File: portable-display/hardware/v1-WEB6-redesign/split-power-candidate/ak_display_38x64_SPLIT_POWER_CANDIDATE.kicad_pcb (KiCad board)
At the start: 4 copper layers, 38 x 64 mm, 125 parts, among them J1 USB4105-GF-A-060, J2 1S LiPo + NTC, J3 DEBUG POGO, J4 KD024EGOIN152-01, J5 MicroSD, Q1 2N7002, Q2 2N7002, Q3 AO3401A, SW1 UP, SW2 DOWN, SW3 OK, SW4 BACK, SW5 POWER, SW6 FEL, U1 AXP2101, U10 TPS65631DPDR, U11 SN74LVC2G17DBVR, U2 V851s, U4 LIS2DW12TR, U5 RV-3028-C7, U6 SN74LVC1G123DCTR, U8 TPS22918DBVR, U9 USBLC6-2SC6, Y1 24MHz 10ppm

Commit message: fix(pcb): add C53 1uF (C52923) + C54 100nF (C1525) at U8 TPS22918 VIN
Both JLC basic 0402, F.Cu, GND via outside pad (>=0.15 mm pad-to-hole).
Schematic regenerated; DRC/parity/ERC 0.
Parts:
- added C53: 1u, Sameat:0402, F.Cu at (5.47, 35.1)
- added C54: 100n, Sameat:0402, F.Cu at (2.75, 36.4)
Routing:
- net GND: track 14.4 -> 16.3 mm, vias 60 -> 62
- net 3V3: track 161.2 -> 161.9 mm

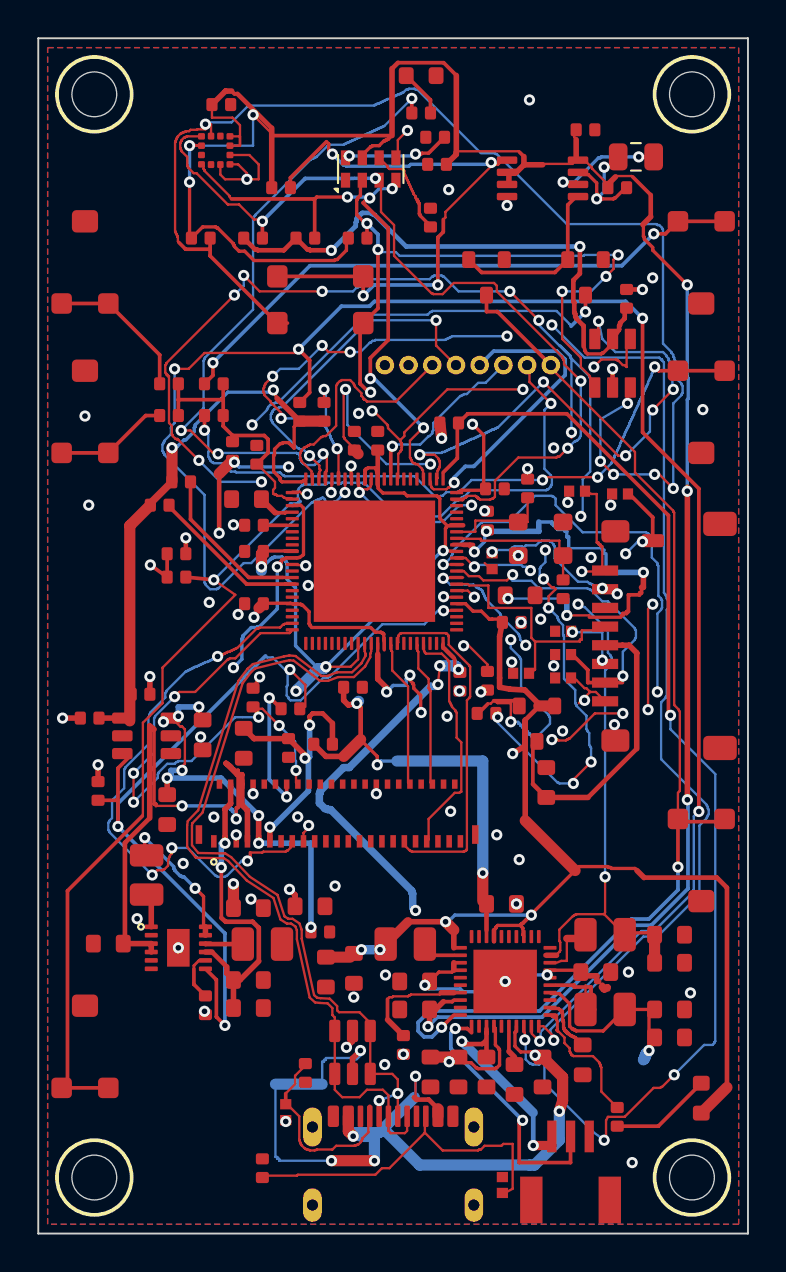
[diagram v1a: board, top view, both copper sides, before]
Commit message: feat(j5): swap microSD to in-stock XKTF-0803-0, TPD4E05U06 flow-through ESD, reroute SD bus off Y1
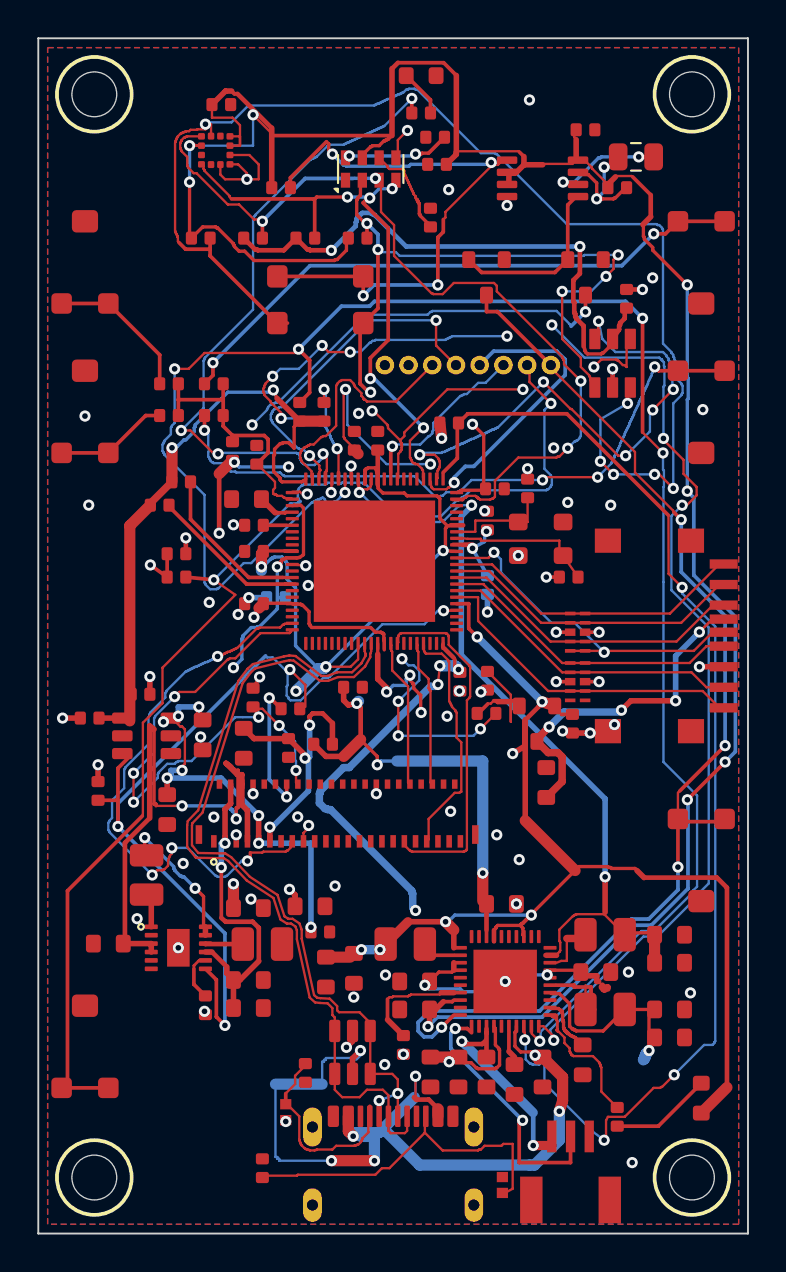
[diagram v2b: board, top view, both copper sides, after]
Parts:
- removed D10, D11, D12, D6, D7, D8, D9: ESDLC5V0LB, Sameat:DFN1006-2
- added C57: 100n, Sameat:0402, B.Cu at (12.7, 29.9)
- added U12: TPD4E05U06DQAR, Sameat:TPD4E05U06_DQA, F.Cu at (28.9, 31.8)
- added U13: TPD4E05U06DQAR, Sameat:TPD4E05U06_DQA, F.Cu at (28.9, 34.5)
- C34: footprint Sameat:0603 -> Sameat:0402; moved to B.Cu
- J5: footprint Sameat:MICROSD -> Sameat:XKTF-0803-0
- moved C14 6.32 mm to (28.6, 36.7), turned to 90 degrees
- moved C34 1.83 mm to (24.1, 29.3), turned to -90 degrees
- moved J5 1.10 mm to (33.6, 32.0)
- moved C13 0.72 mm to (28.4, 28.9), turned to 180 degrees
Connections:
- C14 pad 1: 3V3 -> GND
- C14 pad 2: GND -> 3V3
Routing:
- net SD_PWR_EN: track 79.2 -> 22.1 mm, vias 16 -> 5
- net SOC_LDO_1V8: track 26.7 -> 5.31 mm, vias 5 -> 2
- net SD_D0: track 34.3 -> 16.5 mm, vias 8 -> 0
- net SD_D2: track 31.5 -> 16.5 mm, vias 3 -> 0
- net SD_PWR_GATE: track 18.3 -> 7.96 mm, vias 3 -> 0
- net GND: track 16.3 -> 23.6 mm, vias 62 -> 67
- net DRAM_1V5: track 54.1 -> 58.7 mm, vias 7 -> 5
- net SD_DET: track 15.3 -> 19.5 mm, vias 4 -> 2
- net SD_CLK: track 13.4 -> 16.4 mm
- net SD_CMD: track 14.1 -> 16.5 mm, vias 4 -> 0
- net SD_D1: track 15.3 -> 17.5 mm, vias 2 -> 0
- net PWRON_N: track 59.0 -> 61.0 mm, vias 2 -> 4
- net SD_D3: track 18.3 -> 16.3 mm, vias 2 -> 0
- net RTC_3V3: track 130.5 -> 132.5 mm, vias 7 -> 8
- net SD_3V3: track 16.3 -> 17.6 mm, vias 0 -> 4
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
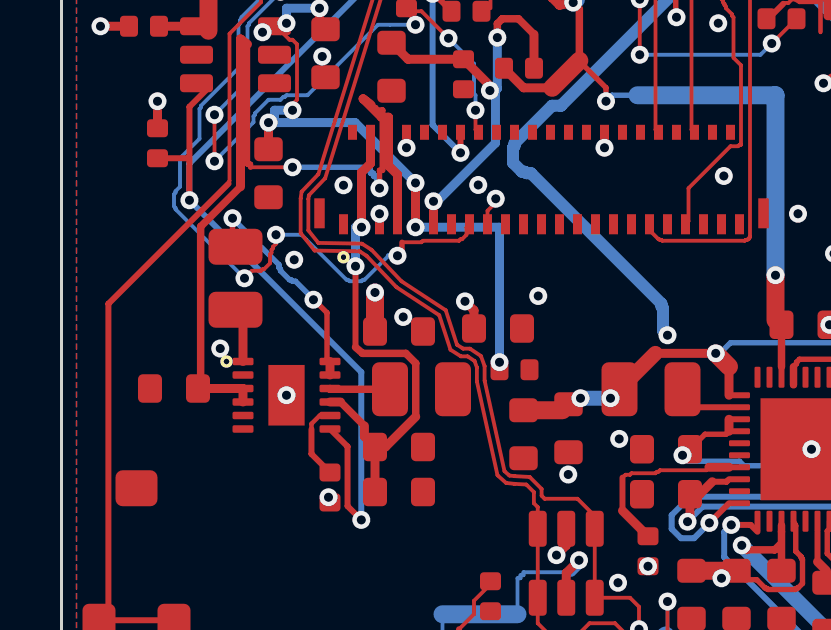
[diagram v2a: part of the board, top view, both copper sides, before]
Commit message: fix(power): feed U10 TPS65631 from 3V3 via local In2 taps; 2x10u+100n under U10
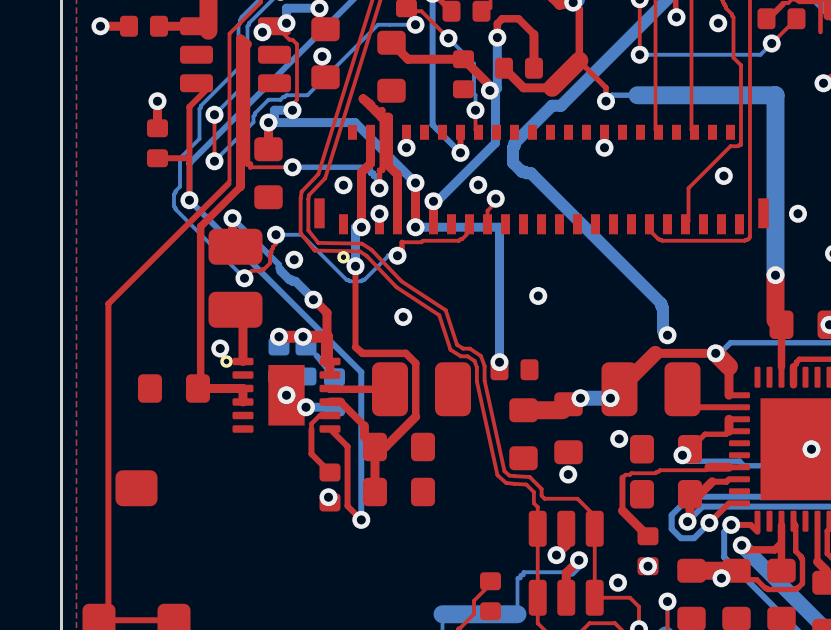
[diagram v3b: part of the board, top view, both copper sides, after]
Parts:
- added C59: 100n, Sameat:0402, B.Cu at (7.25, 47.6)
- C46, C47: footprint Sameat:0603 -> Sameat:0402; moved to B.Cu
- moved C47 5.85 mm to (9.10, 48.6), turned to 90 degrees
- moved C46 3.26 mm to (8.15, 47.6), turned to 90 degrees
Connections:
- C46 pad 1: VSYS -> GND
- C46 pad 2: GND -> 3V3
- C47 pad 1: VSYS -> GND
- C47 pad 2: GND -> 3V3
- L5 pad 1: VSYS -> 3V3
- U10 pad 11: VSYS -> 3V3
- U10 pad 12: VSYS -> 3V3
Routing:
- net 3V3: track 161.6 -> 173.4 mm, vias 19 -> 23
- net VSYS: track 29.3 -> 19.3 mm, vias 7 -> 3
- net GND: track 23.6 -> 24.5 mm, vias 67 -> 68

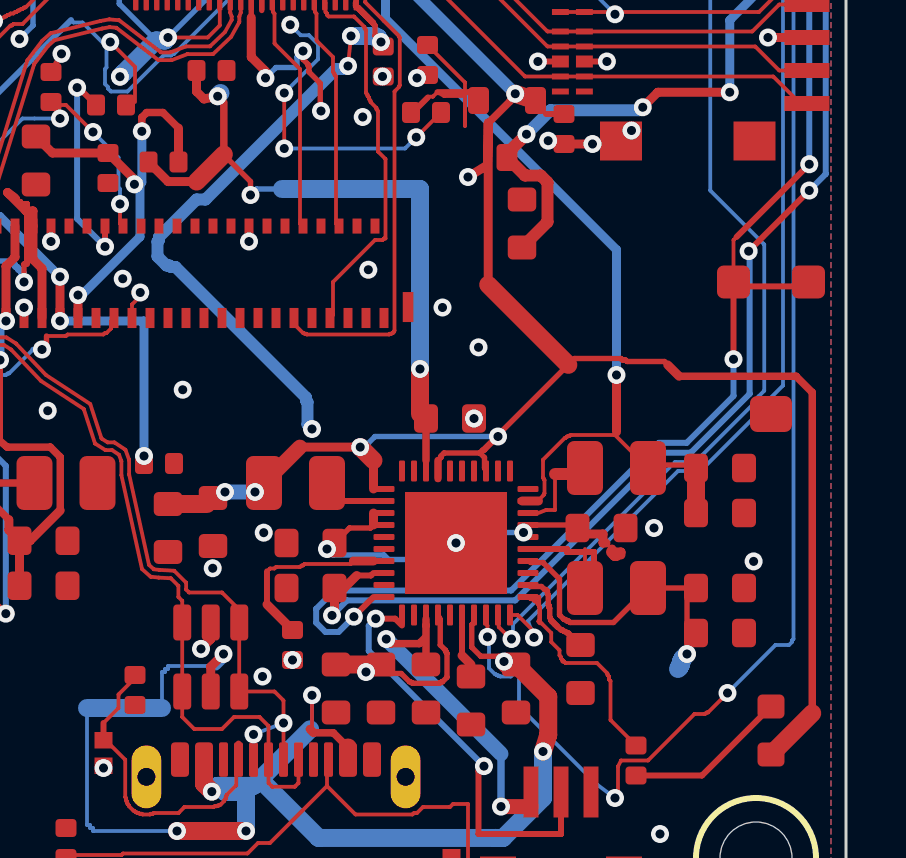
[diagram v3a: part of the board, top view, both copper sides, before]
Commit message: feat(power): 0R bring-up isolation links on AXP2101 rails
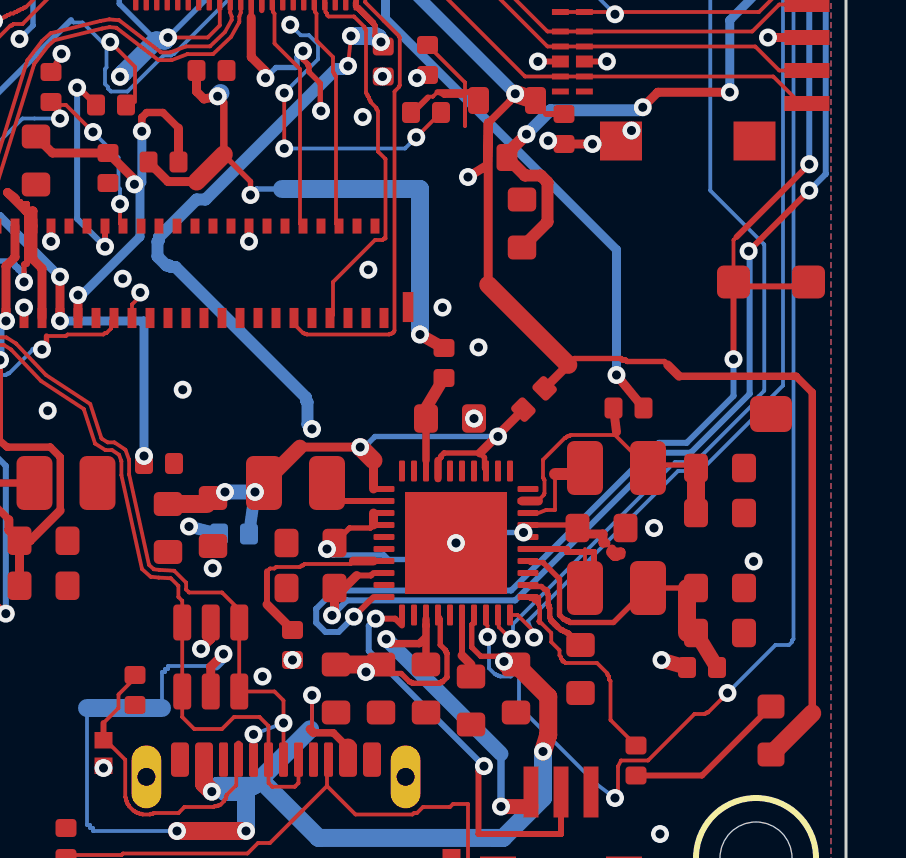
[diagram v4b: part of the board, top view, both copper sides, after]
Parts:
- added R36: 0R, Sameat:0402, F.Cu at (33.2, 54.6)
- added R37: 0R, Sameat:0402, F.Cu at (30.8, 46.0)
- added R38: 0R, Sameat:0402, F.Cu at (27.6, 45.7)
- added R39: 0R, Sameat:0402, B.Cu at (17.6, 50.2)
- added R40: 0R, Sameat:0402, F.Cu at (24.6, 44.5)
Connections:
- C10 pad 1: 1V8 -> 1V8_PMIC
- C14 pad 2: 3V3 -> 3V3_B
- C4 pad 1: 3V3 -> 3V3_PMIC
- C5 pad 1: 3V3 -> 3V3_PMIC
- C6 pad 1: CORE_0V93 -> CORE_0V93_PMIC
- C7 pad 1: CORE_0V93 -> CORE_0V93_PMIC
- C8 pad 1: DRAM_1V5 -> DRAM_1V5_PMIC
- C9 pad 1: DRAM_1V5 -> DRAM_1V5_PMIC
- D1 pad 1: 3V3 -> 3V3_B
- L1 pad 2: 3V3 -> 3V3_PMIC
- L2 pad 2: CORE_0V93 -> CORE_0V93_PMIC
- L3 pad 2: DRAM_1V5 -> DRAM_1V5_PMIC
- Q3 pad 2: 3V3 -> 3V3_B
- U1 pad 13: 3V3 -> 3V3_PMIC
- U1 pad 17: 3V3 -> 3V3_PMIC
- U1 pad 18: 1V8 -> 1V8_PMIC
- U1 pad 21: 3V3 -> 3V3_PMIC
- U1 pad 4: CORE_0V93 -> CORE_0V93_PMIC
- U1 pad 9: DRAM_1V5 -> DRAM_1V5_PMIC
- U2 pad 5: 3V3 -> 3V3_B
- U2 pad 78: 3V3 -> 3V3_B
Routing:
- net 3V3: track 173.4 -> 98.7 mm, vias 23 -> 14
- net 3V3_B: track 0.00 -> 56.6 mm, vias 0 -> 6
- net 3V3_PMIC: track 0.00 -> 19.6 mm, vias 0 -> 4
- net DRAM_1V5_PMIC: track 0.00 -> 10.6 mm
- net DRAM_1V5: track 58.7 -> 48.5 mm
- net CORE_0V93_PMIC: track 0.00 -> 9.67 mm
- net CORE_0V93: track 67.4 -> 58.7 mm
- net 1V8: track 43.0 -> 39.9 mm
- net 1V8_PMIC: track 0.00 -> 2.57 mm
- net GND: vias 68 -> 67

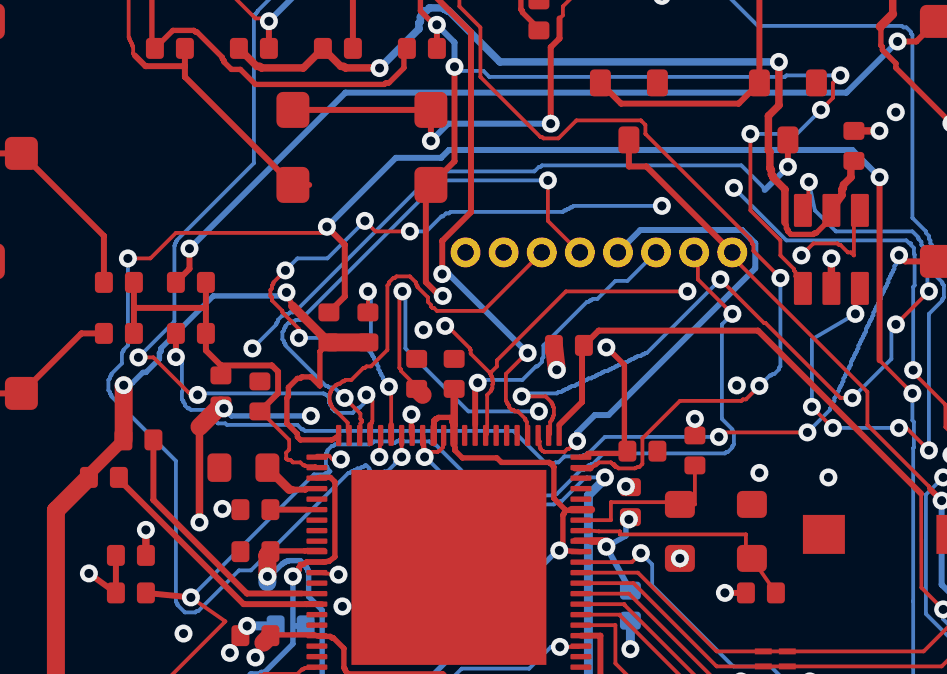
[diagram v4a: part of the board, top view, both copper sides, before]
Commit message: feat(pcb): add B-side decoupling for U2 pins 44/37, reroute low-speed GPIO
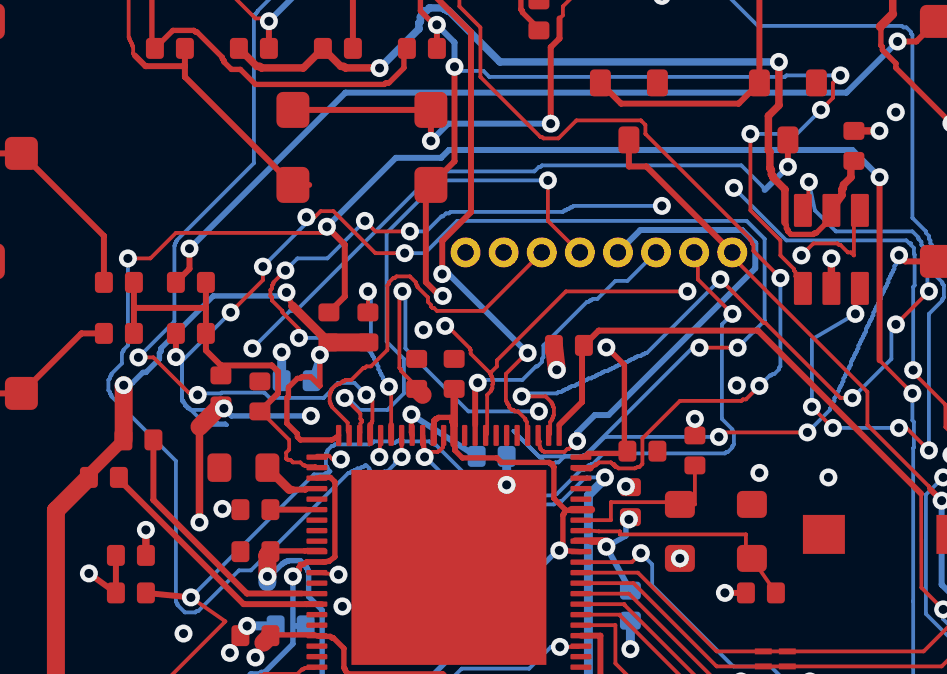
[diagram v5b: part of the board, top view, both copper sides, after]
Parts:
- added C60: 100n, Sameat:0402, B.Cu at (12.9, 21.8)
- added C62: 100n, Sameat:0402, B.Cu at (19.4, 24.3)
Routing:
- net KEY_BACK: track 35.6 -> 65.6 mm, vias 4 -> 10
- net 1V8: track 39.9 -> 42.2 mm
- net GND: track 24.5 -> 26.4 mm, vias 67 -> 69
- net 3V3: track 98.7 -> 99.6 mm, vias 14 -> 15
